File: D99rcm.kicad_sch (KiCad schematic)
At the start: 7 parts, among them Q1A BC847BDW1, Q1B BC847BDW1, Q2A BC857BDW1, Q2B BC857BDW1

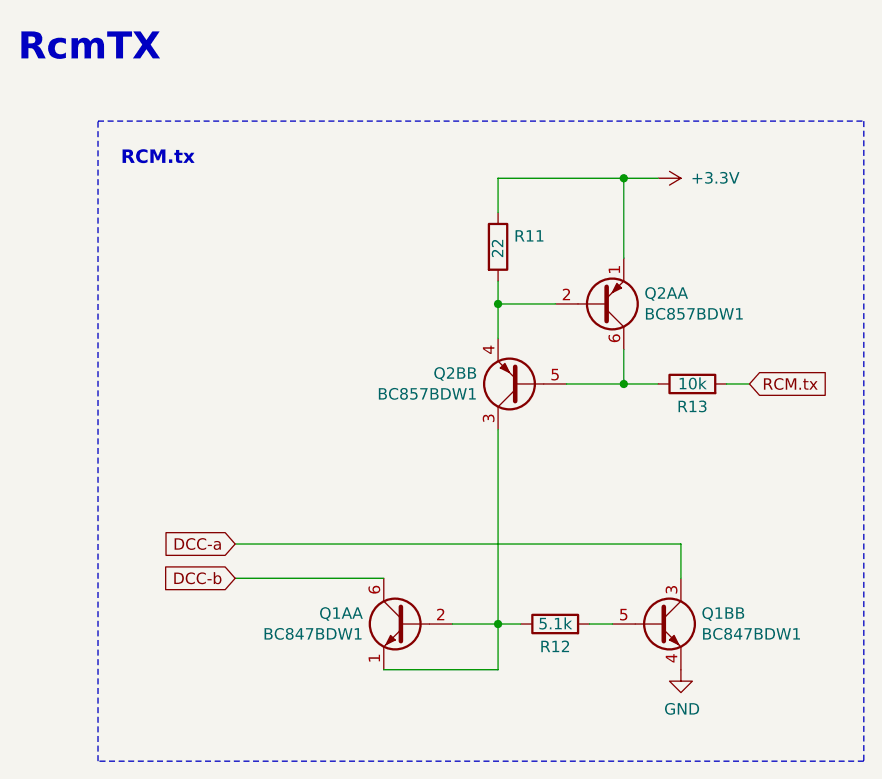
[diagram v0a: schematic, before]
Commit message: mod: ncap leakage resistor
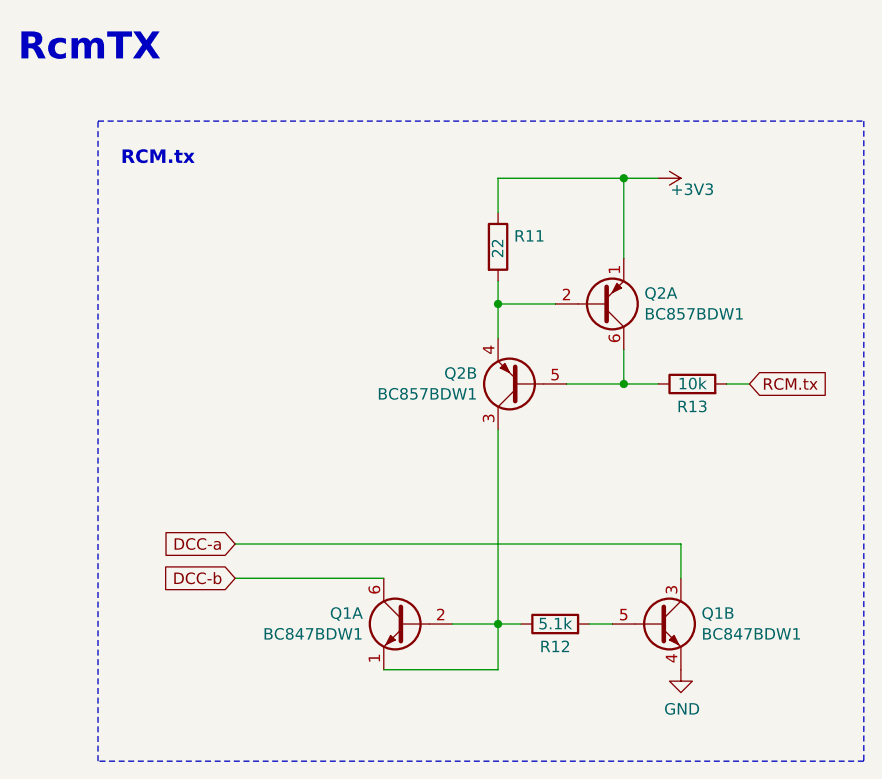
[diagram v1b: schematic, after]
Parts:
- Q1: renamed from Q1A; JLCPCB C82368 -> (none)
- Q2: renamed from Q2A; JLCPCB C383198 -> (none)
- renumbered Q1B to Q1, Q2B to Q2
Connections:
- net +3.3V renamed +3V3
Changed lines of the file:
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@@
 		(on_board yes)
 		(dnp no)
-		(property "Reference" "Q2A"
+		(property "Reference" "Q2"
 			(at 86.106 45.8216 0)
 			(effects
@@
 			)
 		)
-		(property "Description" "-55℃~+150℃ 100MHz 100mA 150@2.0mA,5.0V 15nA 250mW 45V 5V 650mV PNP SOT-363(SC-88) Bipolar (BJT) ROHS"
+		(property "Description" ""
 			(at 81.28 46.99 0)
 			(effects
@@
 			)
 		)
-		(property "JLCPCB" "C383198"
-			(at 81.28 46.99 0)
-			(effects
-				(font
-					(size 1.27 1.27)
-				)
-				(hide yes)
-			)
-		)
 		(pin "4"
 		)
@@
 			(project "D99"
 				(path "/df79ce8b-a870-46f6-824c-d442122538ae/00000000-0000-0000-0000-00005b6d3404"
-					(reference "Q2A")
+					(reference "Q2")
 					(unit 1)
 				)
@@
 		(on_board yes)
 		(dnp no)
-		(property "Reference" "Q2B"
+		(property "Reference" "Q2"
 			(at 67.5386 54.7116 0)
 			(effects
@@
 			(project "D99"
 				(path "/df79ce8b-a870-46f6-824c-d442122538ae/00000000-0000-0000-0000-00005b6d3404"
-					(reference "Q2B")
+					(reference "Q2")
 					(unit 2)
 				)
@@
 		(on_board yes)
 		(dnp no)
-		(property "Reference" "Q1A"
+		(property "Reference" "Q1"
 			(at 54.8386 81.3816 0)
 			(effects
@@
 			)
 		)
-		(property "Description" "-55℃~+150℃ 100MHz 100mA 150@10uA,5.0V 250mV 380mW 45V 5uA NPN SOT-363 Bipolar (BJT) ROHS"
+		(property "Description" ""
 			(at 59.69 82.55 0)
 			(effects
@@
 			)
 		)
-		(property "JLCPCB" "C82368"
-			(at 59.69 82.55 0)
-			(effects
-				(font
-					(size 1.27 1.27)
-				)
-				(hide yes)
-			)
-		)
 		(pin "5"
 		)
@@
 			(project "D99"
 				(path "/df79ce8b-a870-46f6-824c-d442122538ae/00000000-0000-0000-0000-00005b6d3404"
-					(reference "Q1A")
+					(reference "Q1")
 					(unit 1)
 				)
@@
 		(on_board yes)
 		(dnp no)
-		(property "Reference" "Q1B"
+		(property "Reference" "Q1"
 			(at 92.456 81.3816 0)
 			(effects
@@
 			(project "D99"
 				(path "/df79ce8b-a870-46f6-824c-d442122538ae/00000000-0000-0000-0000-00005b6d3404"
-					(reference "Q1B")
+					(reference "Q1")
 					(unit 2)
 				)
@@
 	)
 	(symbol
-		(lib_id "power:+3.3V")
+		(lib_id "power:+3V3")
 		(at 87.63 33.02 270)
 		(unit 1)
@@
 		(on_board yes)
 		(dnp no)
-		(property "Reference" "#PWR0110"
+		(property "Reference" "#PWR01"
 			(at 83.82 33.02 0)
 			(effects
@@
 			)
 		)
-		(property "Value" "+3.3V"
-			(at 93.98 33.02 90)
+		(property "Value" "+3V3"
+			(at 91.44 34.29 90)
 			(effects
 				(font
@@
 			(project "D99"
 				(path "/df79ce8b-a870-46f6-824c-d442122538ae/00000000-0000-0000-0000-00005b6d3404"
-					(reference "#PWR0110")
+					(reference "#PWR01")
 					(unit 1)
 				)

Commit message: mod: refactoring
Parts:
- Q1: LCSC Part # (none) -> C82368
- Q2: LCSC Part # (none) -> C154783
- R11: JLCPCB C25092 -> (none); LCSC Part # (none) -> C25092
- R12: JLCPCB C25905 -> (none); LCSC Part # (none) -> C25905
- R13: JLCPCB C25744 -> (none); LCSC Part # (none) -> C25744
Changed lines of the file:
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@@
 			)
 		)
-		(property "Description" ""
+		(property "Description" "-55℃~+150℃ 100MHz 100mA 2 PNP 220@2.0mA,5.0V 250mW 45V 4uA 5V 650mV PNP SOT-363 Bipolar (BJT) ROHS"
+			(at 81.28 46.99 0)
+			(effects
+				(font
+					(size 1.27 1.27)
+				)
+				(hide yes)
+			)
+		)
+		(property "LCSC Part #" "C154783"
 			(at 81.28 46.99 0)
 			(effects
@@
 			)
 		)
-		(property "Description" ""
+		(property "Description" "-55℃~+150℃ 100MHz 100mA 2 PNP 220@2.0mA,5.0V 250mW 45V 4uA 5V 650mV PNP SOT-363 Bipolar (BJT) ROHS"
 			(at 72.39 55.88 0)
 			(effects
@@
 					(size 1.27 1.27)
 				)
+				(hide yes)
+			)
+		)
+		(property "LCSC Part #" "C154783"
+			(at 72.39 55.88 0)
+			(effects
+				(font
+					(size 1.27 1.27)
+				)
+				(hide yes)
 			)
 		)
@@
 			)
 		)
-		(property "JLCPCB" "C25092"
+		(property "LCSC Part #" "C25092"
 			(at 69.85 40.64 0)
 			(effects
@@
 			)
 		)
-		(property "JLCPCB" "C25744"
+		(property "LCSC Part #" "C25744"
 			(at 91.44 55.88 90)
 			(effects
@@
 			)
 		)
-		(property "Description" ""
+		(property "Description" "-55℃~+150℃ 100MHz 100mA 150@10uA,5.0V 250mV 380mW 45V 5uA NPN SOT-363 Bipolar (BJT) ROHS"
+			(at 59.69 82.55 0)
+			(effects
+				(font
+					(size 1.27 1.27)
+				)
+				(hide yes)
+			)
+		)
+		(property "LCSC Part #" "C82368"
 			(at 59.69 82.55 0)
 			(effects
@@
 			)
 		)
-		(property "JLCPCB" "C25905"
+		(property "LCSC Part #" "C25905"
 			(at 76.2 82.55 90)
 			(effects
@@
 			)
 		)
-		(property "Description" ""
+		(property "Description" "-55℃~+150℃ 100MHz 100mA 150@10uA,5.0V 250mV 380mW 45V 5uA NPN SOT-363 Bipolar (BJT) ROHS"
 			(at 87.63 82.55 0)
 			(effects
@@
 					(size 1.27 1.27)
 				)
-			)
-		)
+				(hide yes)
+			)
+		)
+		(property "LCSC Part #" "C82368"
+			(at 87.63 82.55 0)
+			(effects
+				(font
+					(size 1.27 1.27)
+				)
+				(hide yes)
+			)
+		)
